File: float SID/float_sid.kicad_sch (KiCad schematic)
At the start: 8 parts, among them M4 Continuous Rotation Servo, SW1 Power Switch, U1 Bar02 Depth Sensor

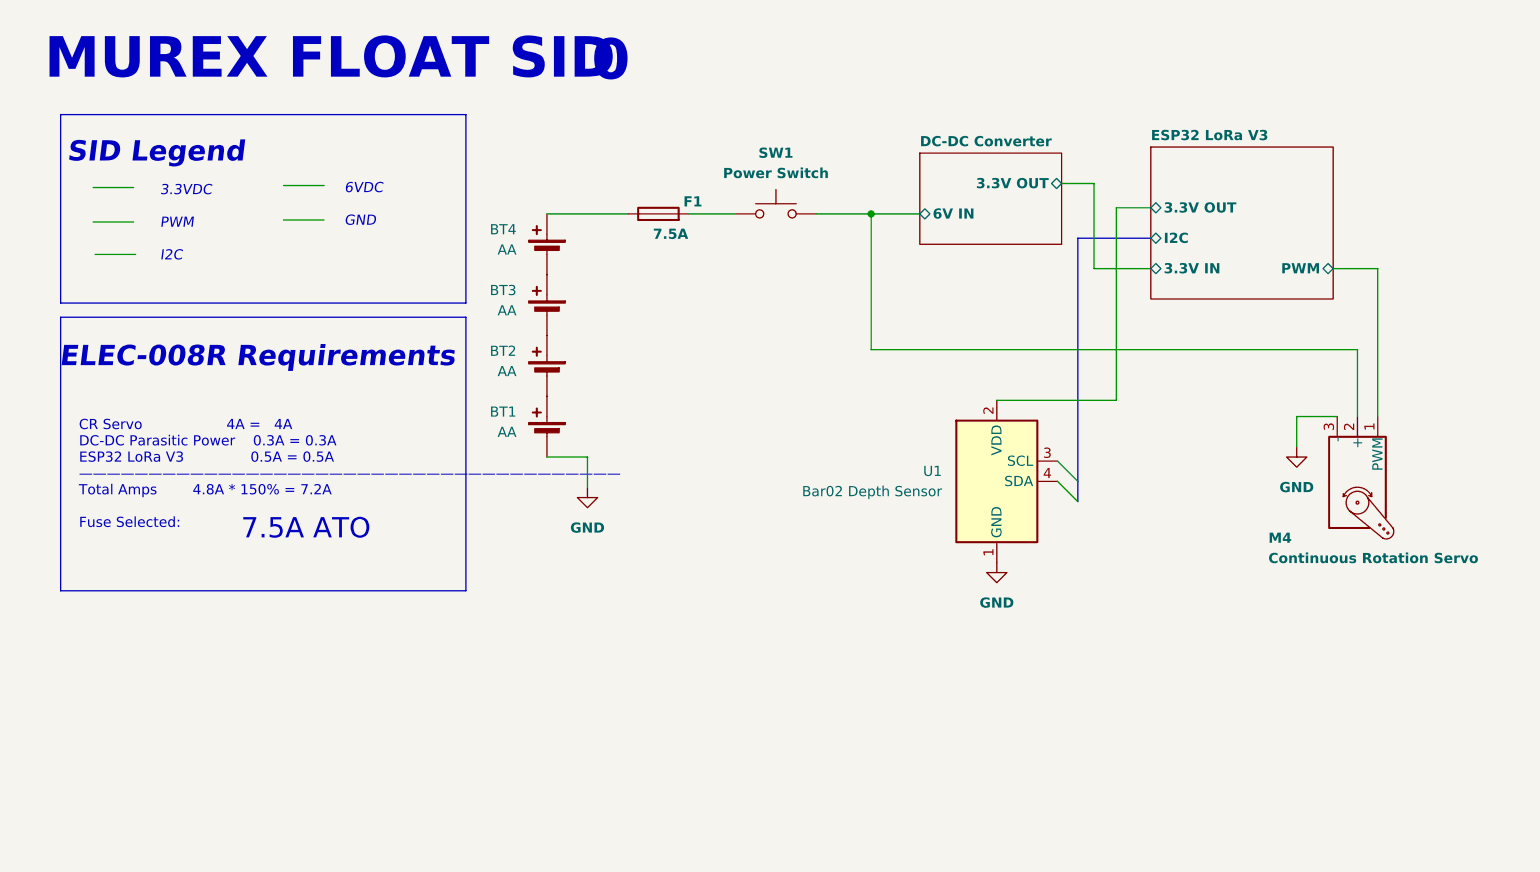
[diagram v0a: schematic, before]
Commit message: feat[card]: worlds business card design
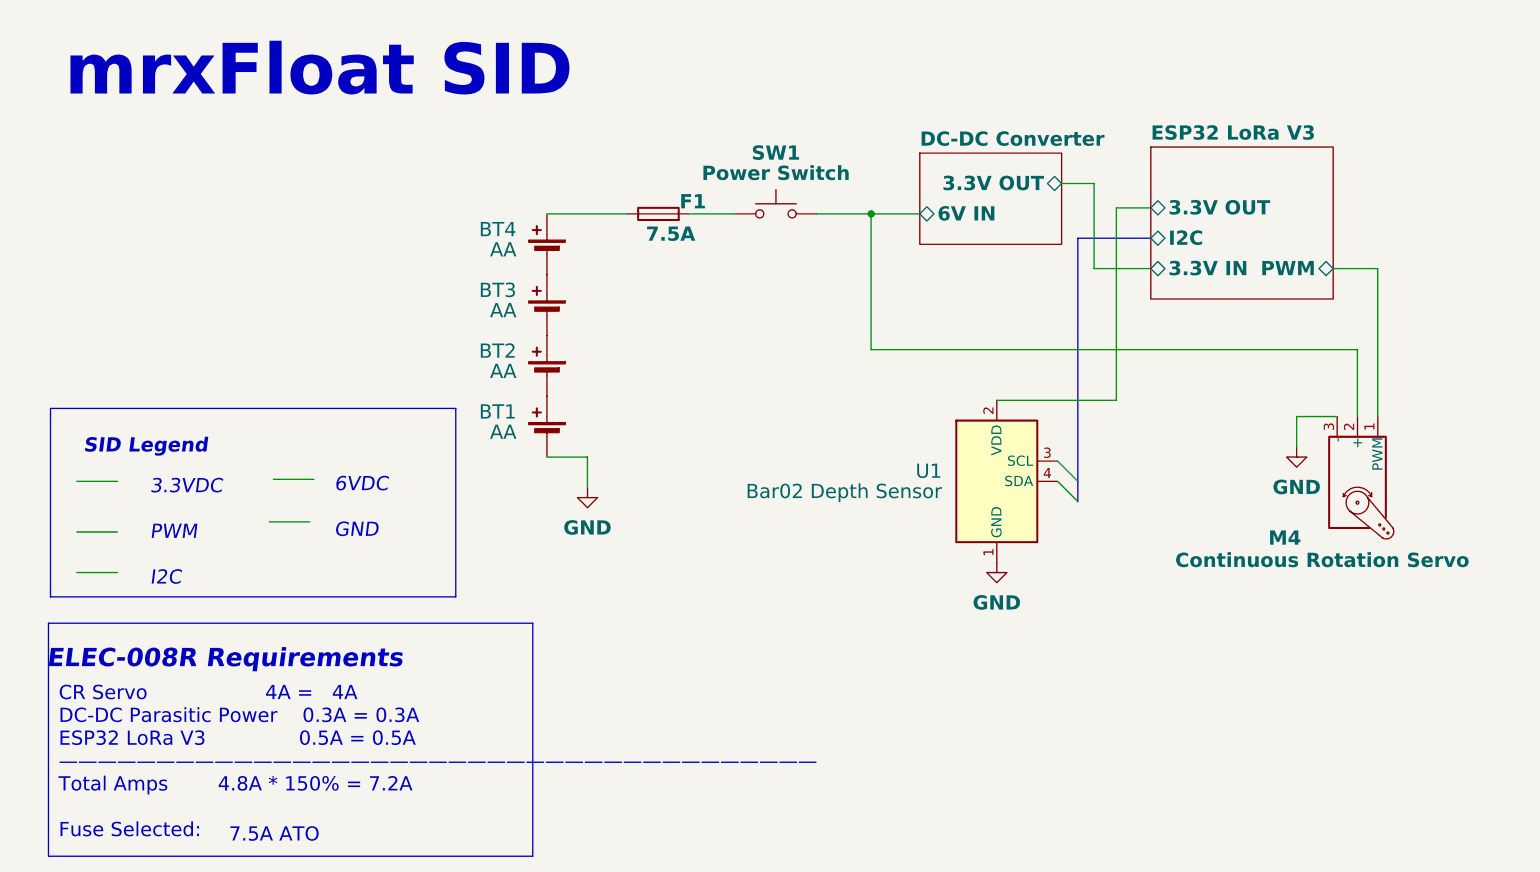
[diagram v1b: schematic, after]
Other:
- note added: "mrxFloat SID"
- note removed: "0"
- note removed: "MUREX FLOAT SID"
